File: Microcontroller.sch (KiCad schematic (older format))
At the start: 50 parts, among them CN1 2x10_Way_2.54mm_Pitch_Header, CN2 CONN_RCPT_USB2.0_MINI_B_SMD_R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, J3 DB1C-A1LD, J4 DB1C-A1LD, J5 DB1C-A1LD, U1 TMP236A4DBZT, U2 STM32L412R8T6, U3 TI_TXB0108PWR, X1 ABM3B-16.000MHZ

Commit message: 2 LCDs (NHD-0216K1Z-FL-YBW) were connected to the FPGA
Connected the two LCDs (NHD-0216K1Z-FL-YBW) to the FPGA through bank 0
Deleted LCD1 and LCD2 that were connected to the microcontroller
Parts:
- removed C13, C14: 100nF_0603_Ceramic_Capacitor,_10%,_X7R,_25V, Capacitor_SMD:C_0603_1608Metric, symbol OpenVent:100nF_0603_Ceramic_Capacitor,_10%,_X7R,_25V
- removed LCD1, LCD2: LCD_MOD_32DIG_16X2_TRANS_YLW_GRN, symbol OpenVent:LCD_MOD_32DIG_16X2_TRANS_YLW_GRN
- removed RV1: RES_trimpot_10K_SMD, Potentiometer_SMD:Potentiometer_Bourns_TC33X_Vertical, symbol OpenVent:RES_trimpot_10K_SMD
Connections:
- net labels removed: LCD-D4, LCD-D5, LCD-D6, LCD-D7, LCD-RS, LCD-RW, LCD-VO
- wire segments 284 -> 230
- no-connect marks 22 -> 14

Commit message: Temp sensor U1 has been removed
Redundant with absolute pressure sensor with temperature RC
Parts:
- removed C2: 100nF_0603_Ceramic_Capacitor,_10%,_X7R,_25V, Capacitor_SMD:C_0603_1608Metric, symbol OpenVent:100nF_0603_Ceramic_Capacitor,_10%,_X7R,_25V
- removed U1: TMP236A4DBZT, Package_TO_SOT_SMD:SOT-23, symbol OpenVent:TMP236A4DBZT
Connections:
- wire segments 230 -> 216
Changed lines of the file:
@@
 Text GLabel 4750 3500 0    50   Input ~ 0
 MOTOR-CURRENT
-$Comp
-L OpenVent:GND #PWR01
-U 1 1 5F8DD176
-P 4575 1250
-F 0 "#PWR01" H 4575 1250 20  0001 C CNN
-F 1 "GND" H 4575 1180 50  0001 C CNN
-F 2 "" H 4575 1250 70  0001 C CNN
-F 3 "" H 4575 1250 70  0001 C CNN
-	1    4575 1250
-	1    0    0    -1
-$EndComp
 Text Label 1800 5100 0    50   ~ 0
 ANALOG-SPARE
@@
 $EndComp
 $Comp
-L OpenVent:3V3 #3V3_04
-U 1 1 5F8DD15A
-P 4575 700
-F 0 "#3V3_04" H 4575 700 20  0001 C CNN
-F 1 "3V3" H 4575 850 50  0000 C CNN
-F 2 "" H 4575 700 70  0001 C CNN
-F 3 "" H 4575 700 70  0001 C CNN
-	1    4575 700
-	1    0    0    -1
-$EndComp
-$Comp
 L OpenVent:+3V3-ALWAYS-ON #3V3-ALWAYS-ON_?
 U 1 1 5F8DD157
@@
 Wire Wire Line
 	2875 2450 2875 2400
-Wire Wire Line
-	4575 1150 4575 1175
-Wire Wire Line
-	4575 850  4575 700
-Wire Wire Line
-	5025 850  4575 850
 Wire Wire Line
 	4975 6825 4325 6825
@@
 $EndComp
 $Comp
-L OpenVent:TMP236A4DBZT U1
-U 1 1 5F8DD13E
-P 5525 950
-F 0 "U1" H 5225 1200 50  0000 L BNN
-F 1 "TMP236A4DBZT" H 5525 700 50  0000 C CNN
-F 2 "Package_TO_SOT_SMD:SOT-23" H 5525 950 50  0001 C CNN
-F 3 "http://www.ti.com/general/docs/suppproductinfo.tsp?distId=10&gotoUrl=http%3A%2F%2Fwww.ti.com%2Flit%2Fgpn%2Ftmp236" H 5525 950 50  0001 C CNN
-F 4 "Texas Instruments" H 5525 950 50  0001 C CNN "Mfr"
-F 5 "TMP236A4DBZT" H 5525 950 50  0001 C CNN "Mfr_PN"
-F 6 "SENSOR TEMPERATURE" H 5525 950 50  0001 C CNN "Desc"
-F 7 "Temperature Sensor Analog, Local -10°C ~ 125°C 19.5mV/°C SOT-23-3" H 5525 950 50  0001 C CNN "Detailed"
-F 8 "DigiKey" H 5525 950 50  0001 C CNN "DistName"
-F 9 "296-TMP236A4DBZTTR-ND" H 5525 950 50  0001 C CNN "Dist_PN"
-	1    5525 950
-	1    0    0    -1
-$EndComp
-$Comp
 L OpenVent:1K_0603_Chip_Resistor,_1%,_0.1W R4
 U 1 1 5F8DD13C
@@
 Connection ~ 1700 3700
 Wire Wire Line
-	3600 1450 3600 1800
-Wire Wire Line
-	3600 1800 4950 1800
-Wire Wire Line
-	6025 950  6175 950
-Wire Wire Line
-	4975 1050 5025 1050
-Wire Wire Line
 	1700 3600 1700 3700
 Wire Wire Line
@@
 Wire Wire Line
 	7000 850  7000 1200
-Connection ~ 4575 850
 Wire Wire Line
 	1450 5300 1450 5350
@@
 	-1   0    0    -1
 $EndComp
-$Comp
-L OpenVent:100nF_0603_Ceramic_Capacitor,_10%,_X7R,_25V C2
-U 1 1 5F8DD13D
-P 4475 1050
-F 0 "C2" V 4625 800 50  0000 L BNN
-F 1 "100nF_0603_Ceramic_Capacitor,_10%,_X7R,_25V" V 4385 860 50  0001 C CNN
-F 2 "Capacitor_SMD:C_0603_1608Metric" H 4385 860 50  0001 C CNN
-F 3 "" H 4385 860 50  0001 C CNN
-F 4 "25V" V 3875 -2050 50  0001 C CNN "Voltage"
-F 5 "10%" H 4475 1050 50  0001 C CNN "Tolerance"
-F 6 "100nF" V 4425 750 50  0000 C CNN "Val"
-	1    4475 1050
-	0    -1   -1   0
-$EndComp
 Text Notes 1550 600  2    50   ~ 0
 SWD Connector
@@
 Wire Wire Line
 	3975 6325 3975 6425
-Wire Wire Line
-	4975 1450 4975 1275
-Wire Wire Line
-	4975 1275 6175 1275
-Wire Wire Line
-	6175 1275 6175 950
-Wire Wire Line
-	3600 1450 4975 1450
-Wire Wire Line
-	4575 1175 4975 1175
-Connection ~ 4575 1175
-Wire Wire Line
-	4575 1175 4575 1250
-Wire Wire Line
-	4975 1175 4975 1050
 $Comp
 L OpenVent:+3V3-ALWAYS-ON #3V3-ALWAYS-ON_?

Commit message: More fixing up of the FPGA symbols, lashed up the sigma delta A/D converter circuitry.  Fixed up the LCD page.  Two displays, two separate enables needed here folks.  FPGA I/O banks power supplies' needs another looking at.  Still lots of stuff to clean up here...
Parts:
- removed U3: TI_TXB0108PWR, Package_SO:TSSOP-20_4.4x6.5mm_P0.65mm, symbol OpenVent:TI_TXB0108PWR
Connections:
- wire segments 216 -> 201
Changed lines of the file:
@@
 Text GLabel 6550 3100 2    50   Output ~ 0
 CE-CONTROL
-$Comp
-L OpenVent:+5V #5V_04
-U 1 1 5F8DD16D
-P 8600 850
-F 0 "#5V_04" H 8600 850 20  0001 C CNN
-F 1 "+5V" H 8600 1000 50  0000 C CNN
-F 2 "" H 8600 850 70  0001 C CNN
-F 3 "" H 8600 850 70  0001 C CNN
-	1    8600 850
-	1    0    0    -1
-$EndComp
-$Comp
-L OpenVent:3V3 #3V3_05
-U 1 1 5F8DD16C
-P 7000 850
-F 0 "#3V3_05" H 7000 850 20  0001 C CNN
-F 1 "3V3" H 7000 1000 50  0000 C CNN
-F 2 "" H 7000 850 70  0001 C CNN
-F 3 "" H 7000 850 70  0001 C CNN
-	1    7000 850
-	1    0    0    -1
-$EndComp
 Text GLabel 4750 3400 0    50   Input ~ 0
 SOUNDER-CURRENT
@@
 Text Label 6500 2800 0    50   ~ 0
 SW-4
-$Comp
-L OpenVent:GND #GND_014
-U 1 1 5F8DD16A
-P 7000 2500
-F 0 "#GND_014" H 7000 2500 20  0001 C CNN
-F 1 "GND" H 7000 2430 50  0001 C CNN
-F 2 "" H 7000 2500 70  0001 C CNN
-F 3 "" H 7000 2500 70  0001 C CNN
-	1    7000 2500
-	1    0    0    -1
-$EndComp
 $Comp
 L OpenVent:GND #PWR02
@@
 Wire Wire Line
 	8450 3500 8450 3600
-Wire Wire Line
-	8600 1200 8600 850
 Wire Wire Line
 	7400 3900 7400 4100
@@
 $EndComp
 $Comp
-L OpenVent:TI_TXB0108PWR U3
-U 1 1 5F8DD149
-P 7100 2500
-F 0 "U3" H 7300 3950 50  0000 L BNN
-F 1 "TI_TXB0108PWR" H 6600 1700 50  0001 L BNN
-F 2 "Package_SO:TSSOP-20_4.4x6.5mm_P0.65mm" H 6600 1700 50  0001 C CNN
-F 3 "http://www.ti.com/general/docs/suppproductinfo.tsp?distId=10&gotoUrl=http%3A%2F%2Fwww.ti.com%2Flit%2Fgpn%2Ftxb0108" H 6600 1700 50  0001 C CNN
-F 4 "Texas Instruments" H 7100 2500 50  0001 C CNN "Mfr"
-F 5 "TXB0108PWR" H 7800 2350 50  0000 C CNN "Mfr_PN"
-F 6 "IC TRNSLTR BIDIRECTIONAL 20TSSOP" H 7100 2500 50  0001 C CNN "Desc"
-F 7 "Voltage Level Translator Bidirectional 1 Circuit 8 Channel 100Mbps 20-TSSOP" H 7100 2500 50  0001 C CNN "Detailed"
-F 8 "DigiKey" H 7100 2500 50  0001 C CNN "DistName"
-F 9 "296-21527-2-ND" H 7100 2500 50  0001 C CNN "Dist_PN"
-	1    7100 2500
-	1    0    0    -1
-$EndComp
-$Comp
 L OpenVent:100nF_0603_Ceramic_Capacitor,_10%,_X7R,_25V C10
 U 1 1 5F8DD148
@@
 	0    -1   -1   0
 $EndComp
-Wire Wire Line
-	7000 850  7000 1200
 Wire Wire Line
 	1450 5300 1450 5350
@@
 	1    0    0    -1
 $EndComp
-Wire Wire Line
-	7100 1200 7000 1200
-Connection ~ 7000 1200
-Wire Wire Line
-	7000 1200 7000 1400
-Wire Wire Line
-	7100 1400 7000 1400
-Wire Wire Line
-	6350 1600 7100 1600
-Wire Wire Line
-	6350 1700 7100 1700
-Wire Wire Line
-	6350 1800 7100 1800
-Wire Wire Line
-	6350 1900 7100 1900
-Wire Wire Line
-	6350 2000 7100 2000
-Wire Wire Line
-	6350 2100 7100 2100
-Wire Wire Line
-	6350 2200 7100 2200
-Wire Wire Line
-	6350 2300 7100 2300
-Wire Wire Line
-	7100 2500 7000 2500
-Wire Wire Line
-	8600 1200 8500 1200
 Text Notes 8900 5800 0    50   ~ 0
 These appear to be placeholders of some sort. ????
@@
 	-1   0    0    -1
 $EndComp
-Text Label 3250 1125 2    50   ~ 0
-SWD-DIO
 Wire Wire Line
 	3075 2600 3075 2800
@@
 Wire Wire Line
 	1425 6025 1425 6700
+Text Label 3250 1125 2    50   ~ 0
+SWD-DIO
 $EndSCHEMATC

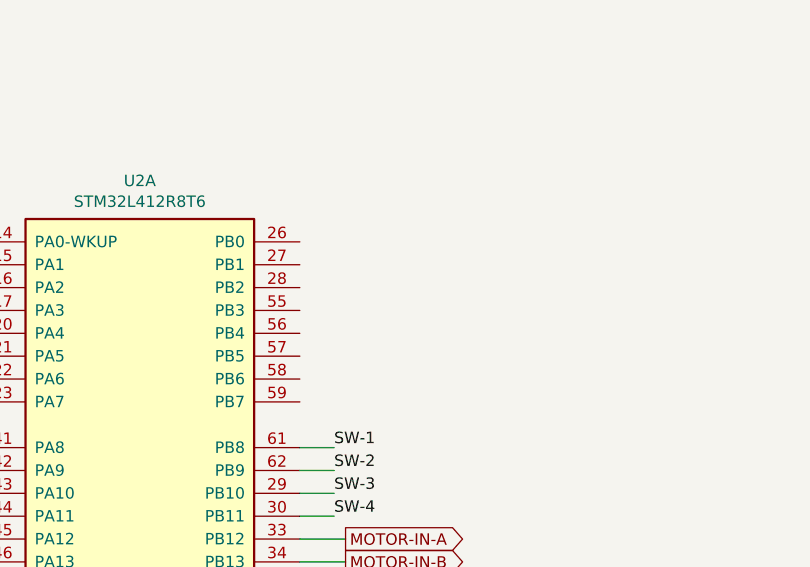
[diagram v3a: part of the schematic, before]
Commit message: Added SPI between FPGA, MCU, sensor
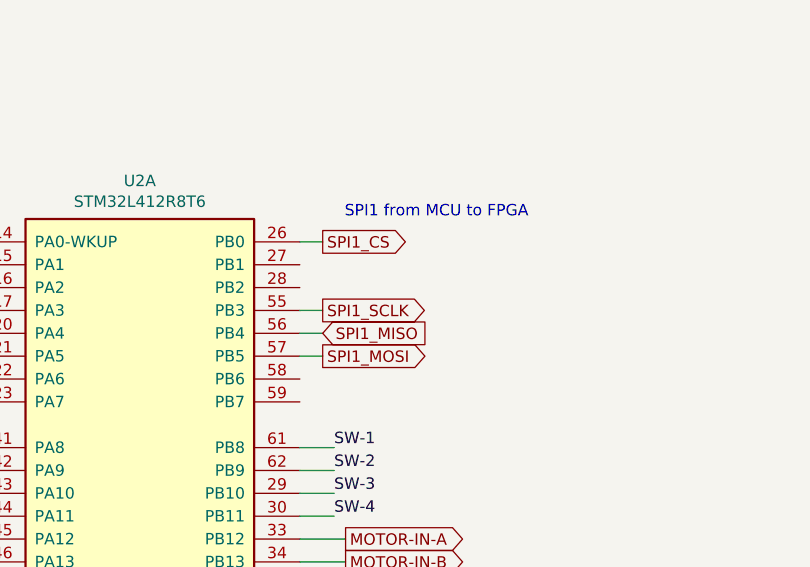
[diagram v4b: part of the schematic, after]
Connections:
- net labels added: SPI1_CS, SPI1_MISO, SPI1_MOSI, SPI1_SCLK
- wire segments 201 -> 205
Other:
- note added: "SPI1 from MCU to FPGA"
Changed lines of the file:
@@
 Text Label 3250 1125 2    50   ~ 0
 SWD-DIO
+Text GLabel 6450 1600 2    50   Output ~ 0
+SPI1_CS
+Text GLabel 6450 1900 2    50   Output ~ 0
+SPI1_SCLK
+Text GLabel 6450 2000 2    50   Input ~ 0
+SPI1_MISO
+Text GLabel 6450 2100 2    50   Output ~ 0
+SPI1_MOSI
+Wire Wire Line
+	6350 1600 6450 1600
+Wire Wire Line
+	6350 1900 6450 1900
+Wire Wire Line
+	6350 2000 6450 2000
+Wire Wire Line
+	6350 2100 6450 2100
+Text Notes 7350 1500 2    50   ~ 0
+SPI1 from MCU to FPGA
 $EndSCHEMATC

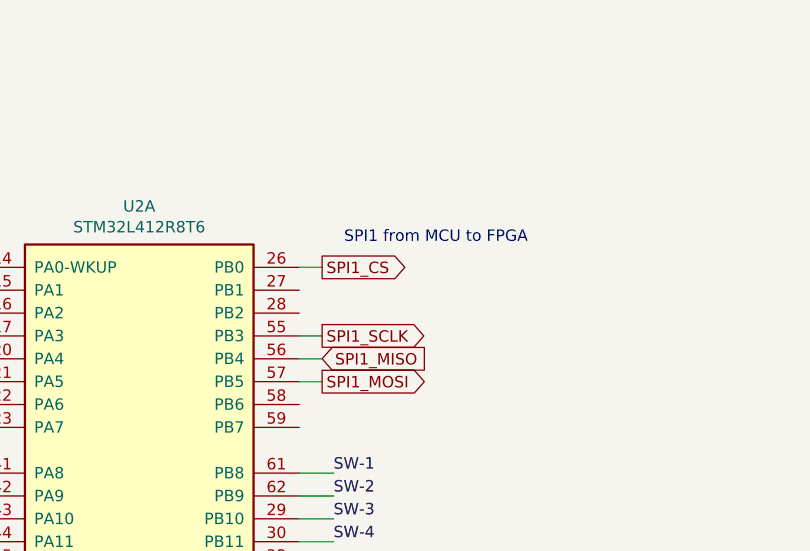
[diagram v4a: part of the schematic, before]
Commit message: SPI from FPGA to MCU and pressure sensor pins changed
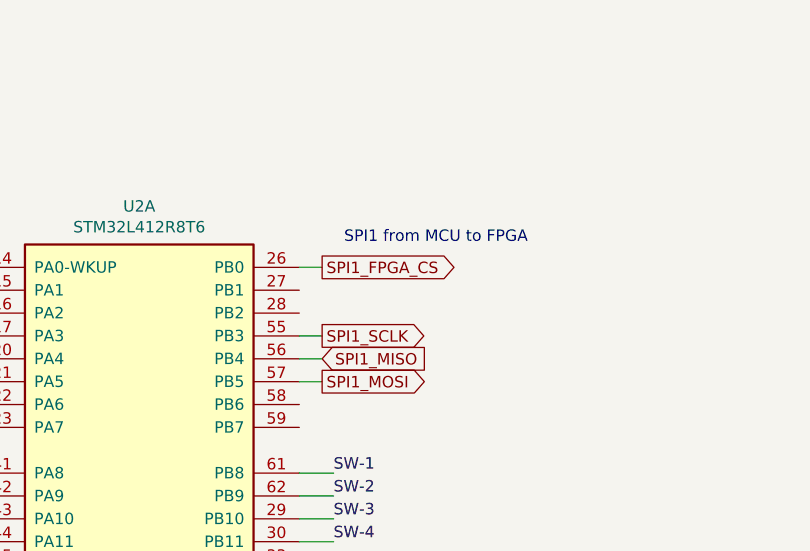
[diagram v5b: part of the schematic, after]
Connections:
- net labels added: SPI1_FPGA_CS
- net labels removed: SPI1_CS
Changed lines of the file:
@@
 SWD-DIO
 Text GLabel 6450 1600 2    50   Output ~ 0
-SPI1_CS
+SPI1_FPGA_CS
 Text GLabel 6450 1900 2    50   Output ~ 0
 SPI1_SCLK

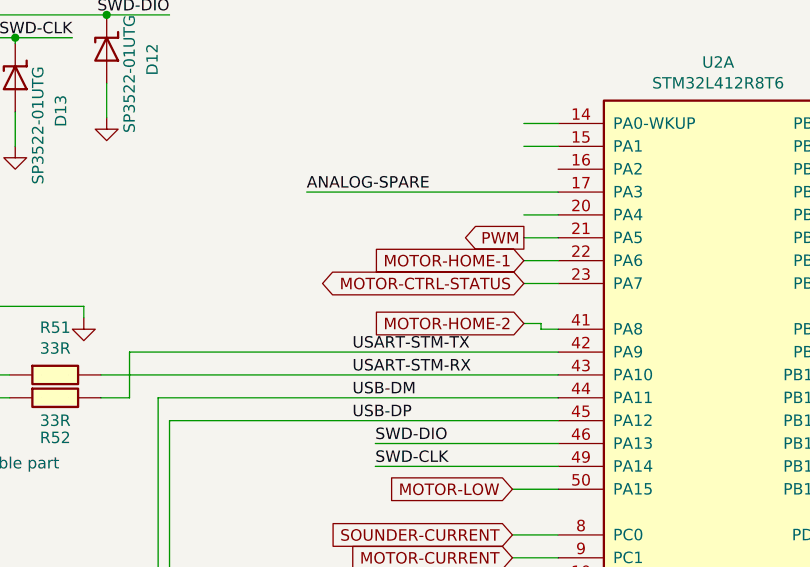
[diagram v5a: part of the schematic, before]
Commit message: Added PWR_UP signal and green LED for Motor Control Status signal to MCU
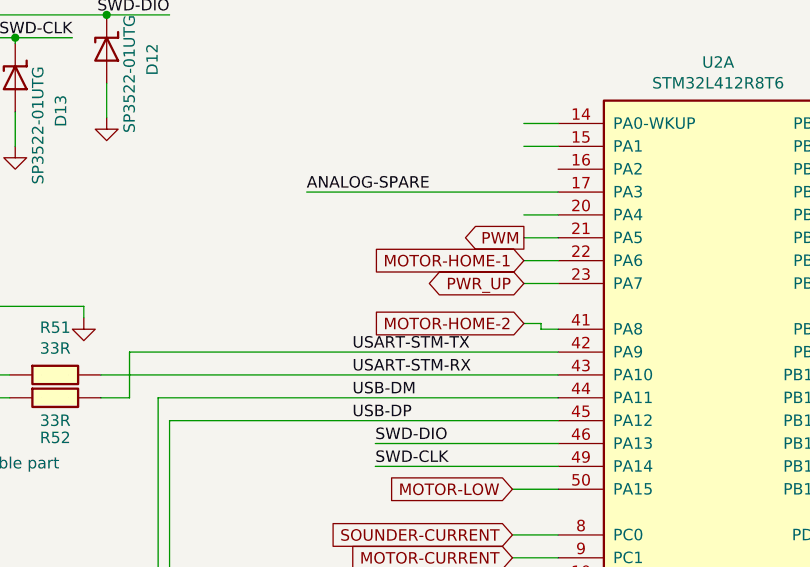
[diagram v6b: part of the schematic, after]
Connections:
- net labels added: PWR_UP
- net labels removed: MOTOR-CTRL-STATUS
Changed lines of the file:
@@
 $EndComp
 Text GLabel 4800 2300 0    50   BiDi ~ 0
-MOTOR-CTRL-STATUS
+PWR_UP
 $Comp
 L OpenVent:+5V #5V_02

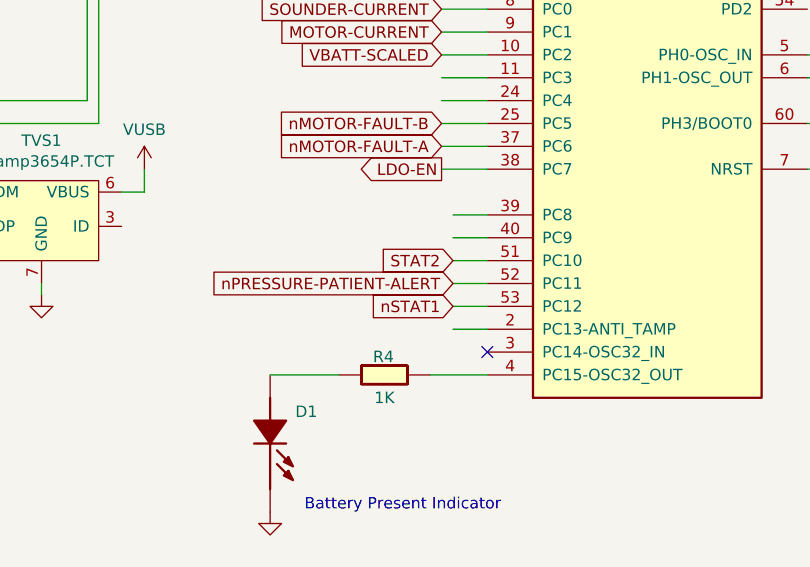
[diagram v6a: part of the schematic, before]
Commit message: Deleted nSTAT1 and STAT2
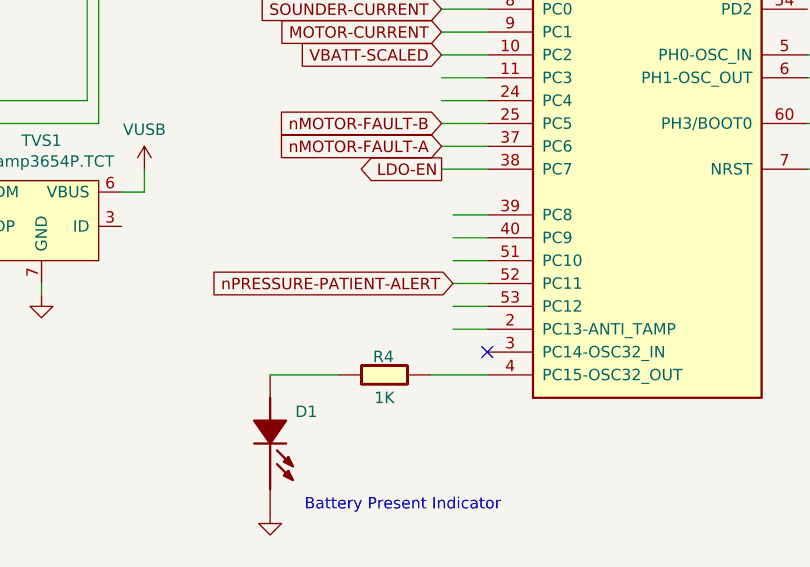
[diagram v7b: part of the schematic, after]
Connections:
- net labels removed: STAT2, nSTAT1
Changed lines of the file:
@@
 Text Notes 4150 5600 0    50   ~ 0
 Battery Present Indicator
-Text GLabel 4800 4500 0    50   Input ~ 0
-STAT2
 Text GLabel 6550 3200 2    50   Input ~ 0
 PGOOD
-Text GLabel 4800 4700 0    50   Input ~ 0
-nSTAT1
 Text GLabel 6550 3100 2    50   Output ~ 0
 CE-CONTROL
